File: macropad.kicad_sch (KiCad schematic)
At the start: 63 parts, among them J1 USB_C_Receptacle_USB2.0, J3 Conn_01x03, J6 Conn_01x04_Pin, J7 Conn_01x02_Pin, J9 Conn_01x02_Pin, SW1 SW_Push, SW3 SW_Push, SW4 SW_Push, SW5 SW_Push, SW6 RotaryEncoder_Switch, SW7 SW_Push, SW8 SW_Push, SW9 RotaryEncoder_Switch, U1 RP2040, U2 W25Q16JVUXIQ, U3 MIC5504-3.3YM5, U6 SN74LVC1T45DRL, U7 USBLC6-2P6, Y1 Crystal_GND24

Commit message: Modifications before initial order.
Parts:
- C29: LCSC C52923 -> C1525
- U7: LCSC C15999 -> C2827693
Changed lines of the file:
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@@
       (effects (font (size 1.27 1.27)) hide)
     )
-    (property "Datasheet" "https://www.st.com/resource/en/datasheet/usblc6-2.pdf" (at 262.89 52.07 0)
-      (effects (font (size 1.27 1.27)) hide)
-    )
-    (property "LCSC" "C15999" (at 259.4611 48.26 0)
+    (property "Datasheet" "" (at 262.89 52.07 0)
+      (effects (font (size 1.27 1.27)) hide)
+    )
+    (property "LCSC" "C2827693" (at 259.4611 48.26 0)
       (effects (font (size 1.27 1.27)) hide)
     )
@@
       (effects (font (size 1.27 1.27)) hide)
     )
-    (property "LCSC" "C52923" (at 80.01 181.6163 0)
+    (property "LCSC" "C1525" (at 80.01 181.6163 0)
       (effects (font (size 1.27 1.27)) hide)
     )
@@
       (effects (font (size 1.27 1.27)) hide)
     )
-    (property "LCSC" "C52923" (at 39.37 181.6163 0)
-      (effects (font (size 1.27 1.27)) hide)
-    )
+    (property "LCSC" "C1525" (at 39.37 181.6163 0)
+      (effects (font (size 1.27 1.27)) hide)
+    )

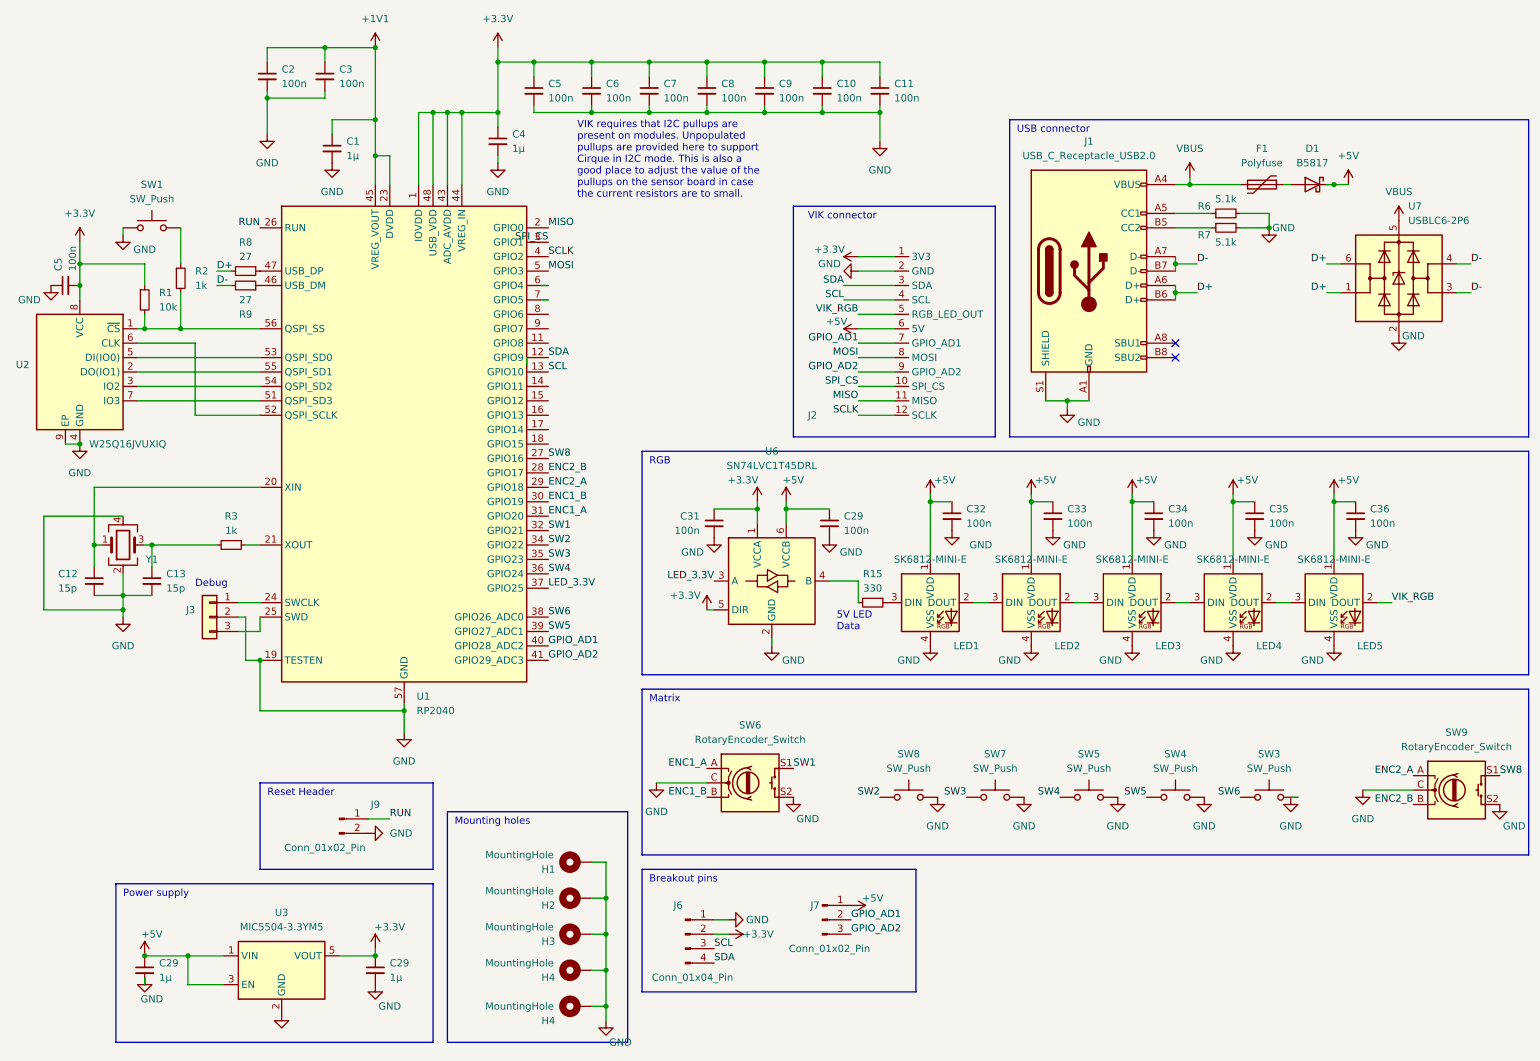
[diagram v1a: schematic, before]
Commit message: I2C pins were incorrect.
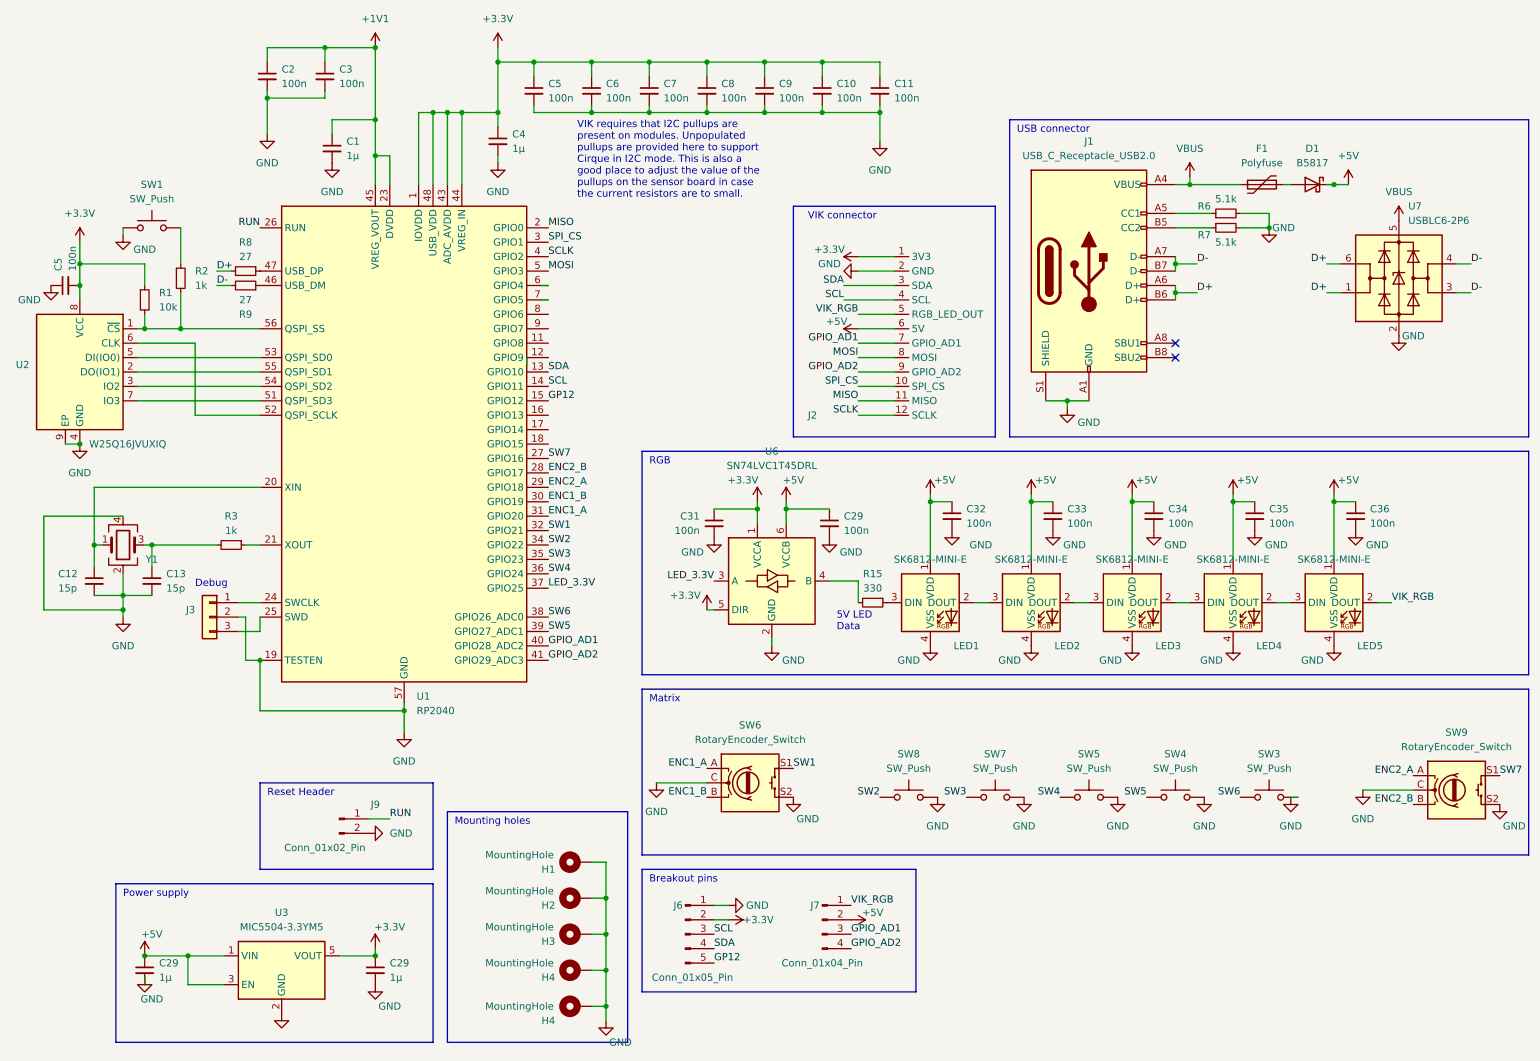
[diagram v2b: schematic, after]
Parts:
- C29: LCSC C1525 -> C52923
- J6: value Conn_01x04_Pin -> Conn_01x05_Pin; footprint Connector_PinHeader_2.54mm:PinHeader_1x04_P2.54mm_Vertical -> Connector_PinHeader_2.54mm:PinHeader_1x05_P2.54mm_Vertical; symbol Connector:Conn_01x04_Pin -> Connector:Conn_01x05_Pin
- J7: value Conn_01x02_Pin -> Conn_01x04_Pin; footprint Connector_PinHeader_2.54mm:PinHeader_1x03_P2.54mm_Vertical -> Connector_PinHeader_2.54mm:PinHeader_1x04_P2.54mm_Vertical; symbol Connector:Conn_01x03_Pin -> Connector:Conn_01x04_Pin
- U6: footprint Package_TO_SOT_SMD:SOT-563 -> Trackpad:SN74LVC1T45DRLR
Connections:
- net +5V: now also J7.2 (Pin_2); no longer J7.1 (Pin_1)
- net GPIO_AD1: now also J7.3 (Pin_3); no longer J7.2 (Pin_2)
- net GPIO_AD2: now also J7.4 (Pin_4); no longer J7.3 (Pin_3)
- net SCL: now also U1.14 (GPIO11); no longer U1.13 (GPIO10)
- net SDA: now also U1.13 (GPIO10); no longer U1.12 (GPIO9)
- net VIK_RGB: now also J7.1 (Pin_1)
- net GP12: now reaches U1.15 (GPIO12)
- net GP12: now also J6.5 (Pin_5)
- net SW8 renamed SW7

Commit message: Fixes for minor issues in the v1.0 PCB.
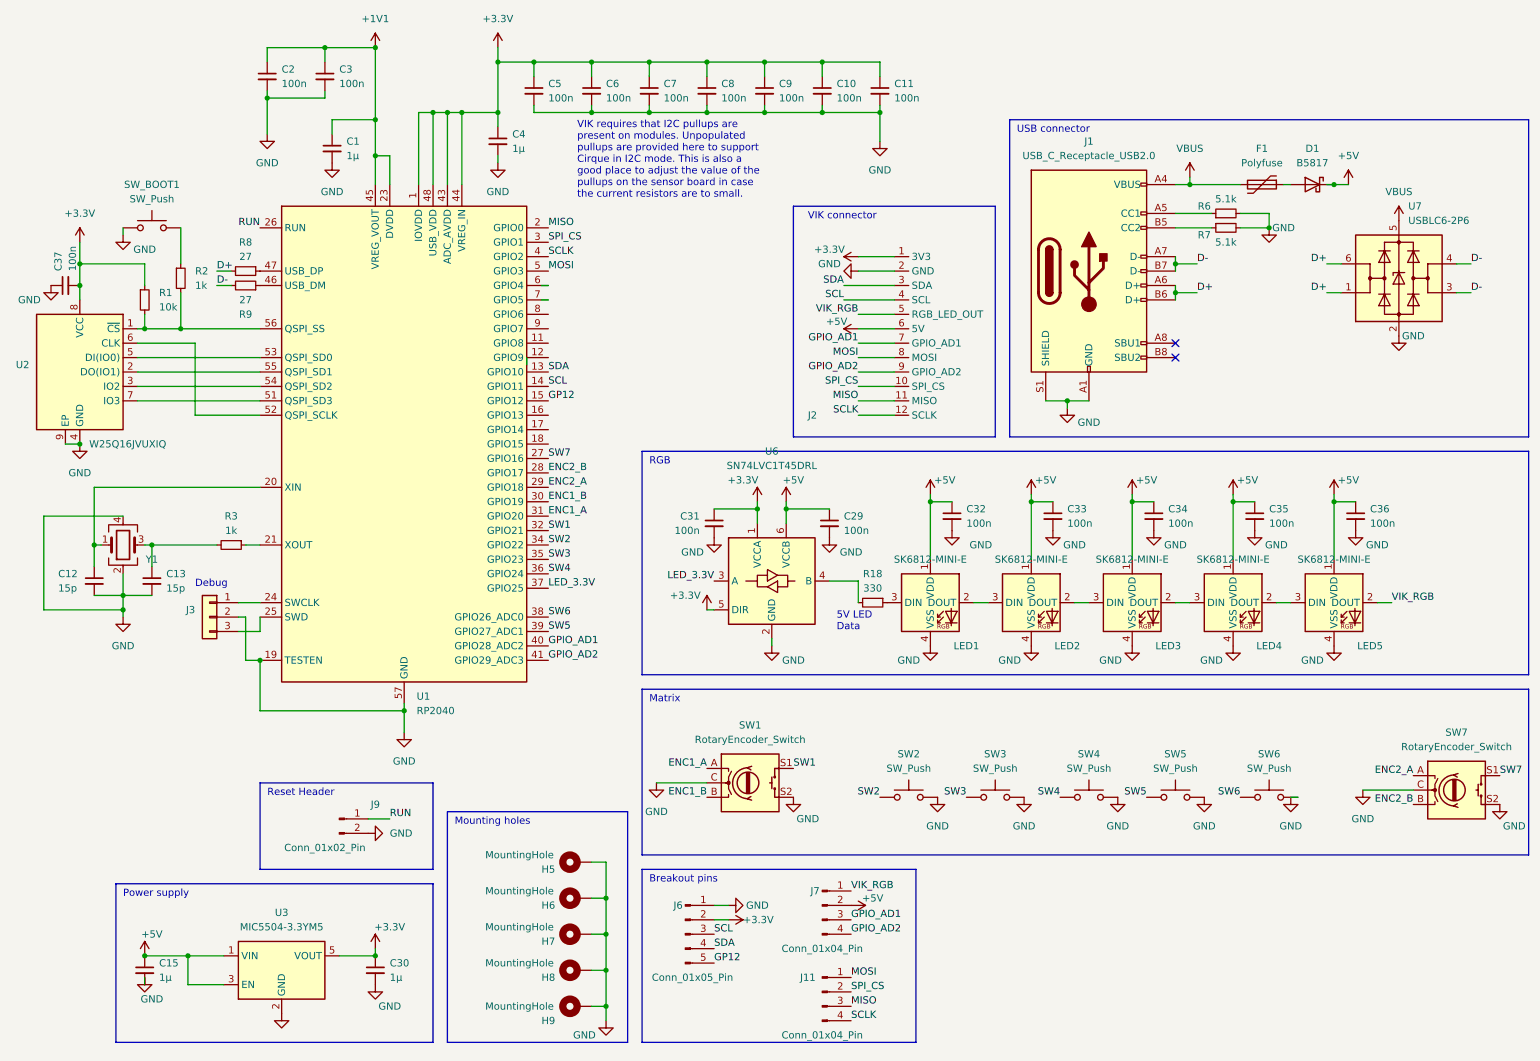
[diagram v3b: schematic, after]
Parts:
- added J11: Conn_01x04_Pin, Connector_PinSocket_1.00mm:PinSocket_1x04_P1.00mm_Vertical, symbol Connector:Conn_01x04_Pin
- SW1: renamed from SW6; footprint PCM_marbastlib-various:ROT_Alps_EC11E-Switch -> Trackpad:ROT_Alps_EC11E-Switch
- SW7: renamed from SW9; footprint PCM_marbastlib-various:ROT_Alps_EC11E-Switch -> Trackpad:ROT_Alps_EC11E-Switch
- renumbered C29 to C15, C29 to C30, C5 to C37, H1 to H5, H2 to H6, H3 to H7, H4 to H8, H4 to H9, R15 to R18, SW8 to SW2, SW7 to SW3, SW5 to SW4, SW4 to SW5, SW3 to SW6, SW1 to SW_BOOT1
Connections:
- net MISO: now also J11.3 (Pin_3)
- net MOSI: now also J11.1 (Pin_1)
- net SCLK: now also J11.4 (Pin_4)
- net SPI_CS: now also J11.2 (Pin_2)
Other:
- moved on the sheet: J7

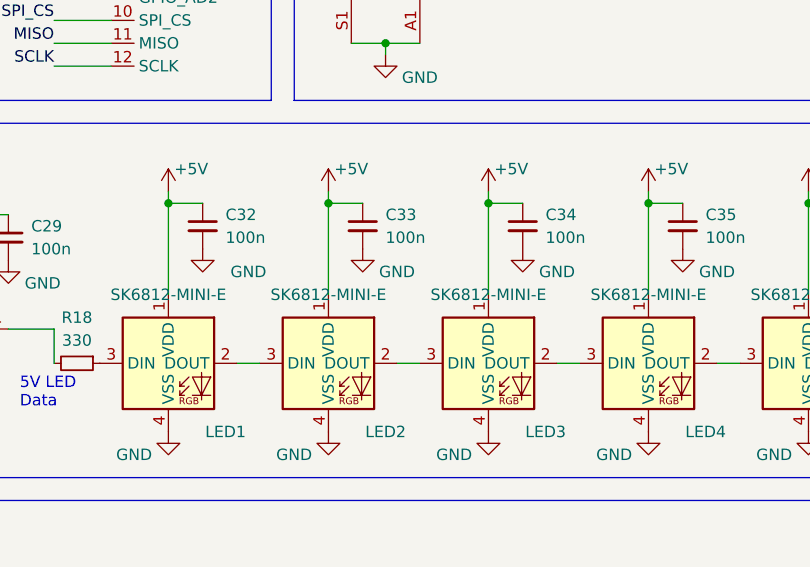
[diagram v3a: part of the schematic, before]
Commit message: Fix minor issues reported by JLC, and replace parts which are often out of stock.
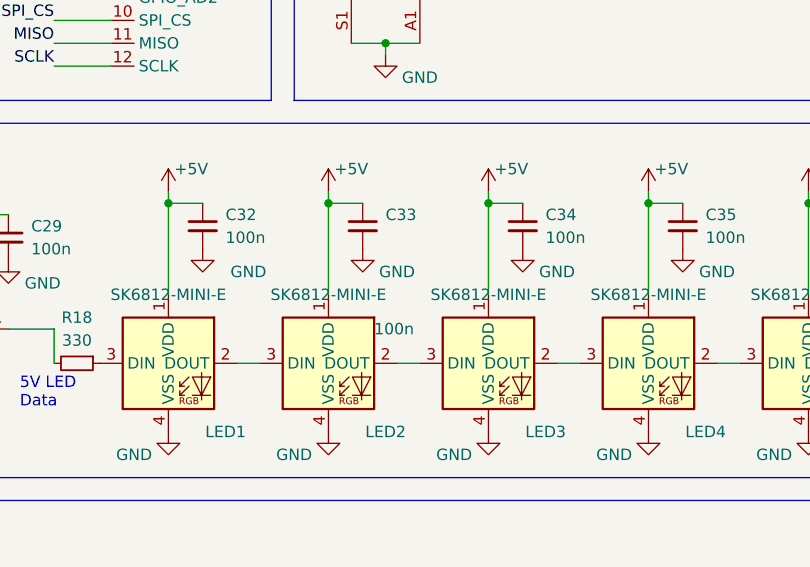
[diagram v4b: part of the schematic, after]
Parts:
- H5, H6, H7, H8, H9, J11, J3, J6, J7, J9, SW1, SW2, SW3, SW4, SW5, SW6, SW7: now left out of the parts list
- J2: LCSC C2919479 -> C2906115
- SW_BOOT1: LCSC C221821 -> C256105
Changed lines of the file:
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@@
   )
   (symbol (lib_id "Connector_Generic:Conn_01x03") (at 48.26 120.65 0) (mirror y) (unit 1)
-    (in_bom yes) (on_board yes) (dnp no)
+    (in_bom no) (on_board yes) (dnp no)
     (property "Reference" "J3" (at 45.72 119.38 0)
       (effects (font (size 1.27 1.27)) (justify left))
@@
   )
   (symbol (lib_id "Device:C_Small") (at 196.85 102.87 0) (unit 1)
-    (in_bom yes) (on_board yes) (dnp no) (fields_autoplaced)
+    (in_bom yes) (on_board yes) (dnp no)
     (property "Reference" "C33" (at 199.39 101.6063 0)
       (effects (font (size 1.27 1.27)) (justify left))
     )
-    (property "Value" "100n" (at 199.39 104.1463 0)
+    (property "Value" "100n" (at 198.12 114.3 0)
       (effects (font (size 1.27 1.27)) (justify left))
     )
@@
   )
   (symbol (lib_id "Mechanical:MountingHole_Pad") (at 113.03 163.83 90) (unit 1)
-    (in_bom yes) (on_board yes) (dnp no)
+    (in_bom no) (on_board yes) (dnp no)
     (property "Reference" "H5" (at 107.95 165.1 90)
       (effects (font (size 1.27 1.27)))
@@
   )
   (symbol (lib_id "Connector:Conn_01x04_Pin") (at 156.21 171.45 0) (unit 1)
-    (in_bom yes) (on_board yes) (dnp no)
+    (in_bom no) (on_board yes) (dnp no)
     (property "Reference" "J7" (at 154.94 168.91 0)
       (effects (font (size 1.27 1.27)))
@@
   )
   (symbol (lib_id "Mechanical:MountingHole_Pad") (at 113.03 176.53 90) (unit 1)
-    (in_bom yes) (on_board yes) (dnp no)
+    (in_bom no) (on_board yes) (dnp no)
     (property "Reference" "H7" (at 107.95 177.8 90)
       (effects (font (size 1.27 1.27)))
@@
   )
   (symbol (lib_id "Connector:Conn_01x02_Pin") (at 71.12 156.21 0) (unit 1)
-    (in_bom yes) (on_board yes) (dnp no)
+    (in_bom no) (on_board yes) (dnp no)
     (property "Reference" "J9" (at 77.47 153.67 0)
       (effects (font (size 1.27 1.27)))
@@
       (effects (font (size 1.27 1.27)) hide)
     )
-    (property "LCSC" "C2919479" (at 153.67 85.09 0)
+    (property "LCSC" "C2906115" (at 153.67 85.09 0)
       (effects (font (size 1.27 1.27)) hide)
     )
@@
   )
   (symbol (lib_id "Device:RotaryEncoder_Switch") (at 143.51 149.86 0) (unit 1)
-    (in_bom yes) (on_board yes) (dnp no) (fields_autoplaced)
+    (in_bom no) (on_board yes) (dnp no) (fields_autoplaced)
     (property "Reference" "SW1" (at 143.51 139.7 0)
       (effects (font (size 1.27 1.27)))
@@
   )
   (symbol (lib_id "Mechanical:MountingHole_Pad") (at 113.03 182.88 90) (unit 1)
-    (in_bom yes) (on_board yes) (dnp no)
+    (in_bom no) (on_board yes) (dnp no)
     (property "Reference" "H8" (at 107.95 184.15 90)
       (effects (font (size 1.27 1.27)))
@@
   )
   (symbol (lib_id "Connector:Conn_01x05_Pin") (at 132.08 176.53 0) (unit 1)
-    (in_bom yes) (on_board yes) (dnp no)
+    (in_bom no) (on_board yes) (dnp no)
     (property "Reference" "J6" (at 130.81 171.45 0)
       (effects (font (size 1.27 1.27)))
@@
   )
   (symbol (lib_id "Mechanical:MountingHole_Pad") (at 113.03 189.23 90) (unit 1)
-    (in_bom yes) (on_board yes) (dnp no)
+    (in_bom no) (on_board yes) (dnp no)
     (property "Reference" "H9" (at 107.95 191.77 90)
       (effects (font (size 1.27 1.27)))
@@
   )
   (symbol (lib_id "Mechanical:MountingHole_Pad") (at 113.03 170.18 90) (unit 1)
-    (in_bom yes) (on_board yes) (dnp no)
+    (in_bom no) (on_board yes) (dnp no)
     (property "Reference" "H6" (at 107.95 171.45 90)
       (effects (font (size 1.27 1.27)))
@@
   )
   (symbol (lib_id "Switch:SW_Push") (at 218.44 152.4 0) (mirror y) (unit 1)
-    (in_bom yes) (on_board yes) (dnp no)
+    (in_bom no) (on_board yes) (dnp no)
     (property "Reference" "SW5" (at 218.44 144.78 0)
       (effects (font (size 1.27 1.27)))
@@
   )
   (symbol (lib_id "Switch:SW_Push") (at 186.69 152.4 0) (mirror y) (unit 1)
-    (in_bom yes) (on_board yes) (dnp no)
+    (in_bom no) (on_board yes) (dnp no)
     (property "Reference" "SW3" (at 186.69 144.78 0)
       (effects (font (size 1.27 1.27)))
@@
       (effects (font (size 1.27 1.27)) hide)
     )
-    (property "LCSC" "C221821" (at 38.1 44.45 0)
+    (property "LCSC" "C256105" (at 38.1 44.45 0)
       (effects (font (size 1.27 1.27)) hide)
     )
@@
   )
   (symbol (lib_id "Switch:SW_Push") (at 203.2 152.4 0) (mirror y) (unit 1)
-    (in_bom yes) (on_board yes) (dnp no)
+    (in_bom no) (on_board yes) (dnp no)
     (property "Reference" "SW4" (at 203.2 144.78 0)
       (effects (font (size 1.27 1.27)))
@@
   )
   (symbol (lib_id "Connector:Conn_01x04_Pin") (at 156.21 186.69 0) (unit 1)
-    (in_bom yes) (on_board yes) (dnp no)
+    (in_bom no) (on_board yes) (dnp no)
     (property "Reference" "J11" (at 153.67 184.15 0)
       (effects (font (size 1.27 1.27)))
@@
   )
   (symbol (lib_id "Switch:SW_Push") (at 234.95 152.4 0) (mirror y) (unit 1)
-    (in_bom yes) (on_board yes) (dnp no)
+    (in_bom no) (on_board yes) (dnp no)
     (property "Reference" "SW6" (at 234.95 144.78 0)
       (effects (font (size 1.27 1.27)))
@@
   )
   (symbol (lib_id "Device:RotaryEncoder_Switch") (at 267.97 151.13 0) (unit 1)
-    (in_bom yes) (on_board yes) (dnp no) (fields_autoplaced)
+    (in_bom no) (on_board yes) (dnp no) (fields_autoplaced)
     (property "Reference" "SW7" (at 267.97 140.97 0)
       (effects (font (size 1.27 1.27)))
@@
   )
   (symbol (lib_id "Switch:SW_Push") (at 171.45 152.4 0) (mirror y) (unit 1)
-    (in_bom yes) (on_board yes) (dnp no)
+    (in_bom no) (on_board yes) (dnp no)
     (property "Reference" "SW2" (at 171.45 144.78 0)
       (effects (font (size 1.27 1.27)))

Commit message: Swap the VIK connector part for the default, the new part has pin 1 labelled differently
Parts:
- J2: LCSC C2906115 -> C479750
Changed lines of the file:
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@@
       (effects (font (size 1.27 1.27)) hide)
     )
-    (property "LCSC" "C2906115" (at 153.67 85.09 0)
+    (property "LCSC" "C479750" (at 153.67 85.09 0)
       (effects (font (size 1.27 1.27)) hide)
     )
